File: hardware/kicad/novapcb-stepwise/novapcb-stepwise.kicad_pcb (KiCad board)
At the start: 6 copper layers, 105 x 85 mm, 129 parts, among them J1 USB-C_2.0, J10 CRSF_solder_pad, J11 ESC_solder_pad, J12 ESC_solder_pad, J13 ESC_solder_pad, J14 ESC_solder_pad, J15 ESC_solder_pad, J16 ESC_solder_pad, J17 ESC_solder_pad, J18 ESC_solder_pad, J19 MAUCH2_6P, J2 microSD_DM3AT, J20 CAN_4P, J3 TELEM_6P, J4 MAUCH_6P, J5 GPS_MAG_10P, J9 SWD_10P, Q2 AO3401A, Q3 AO4262E, Q4 AO4262E, Q5 AO3400A, U1 STM32H743VITx, U11 LM74700-Q1, U12 LM74700-Q1, U13 LP5907MFX-3.3, U14 TJA1051TK/3, U15 PESD2CAN, U2 AP2112K-3.3, U3 ICM-42688-P_LGA-14_2.5x3mm_P0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, U4 DPS310, U5 USBLC6-2P6, U6 TPS25940A, U7 LPS22HB, U8 BMI088, U9 LSM6DSV16X, Y1 8MHz

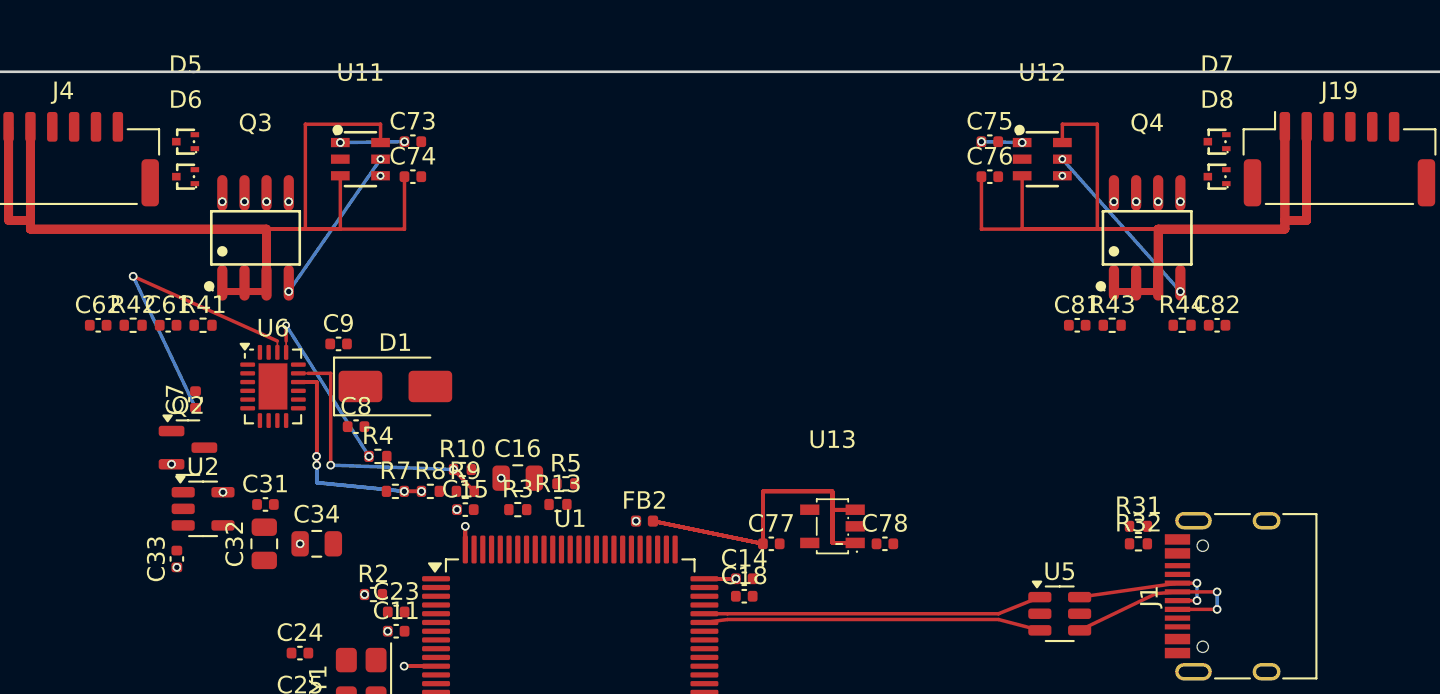
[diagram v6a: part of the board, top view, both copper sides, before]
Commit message: hw: Option B step 3 — U2 area re-layout + 4 sense-row mirror fixes
Per master 2026-05-23 sign-off on sch/option-b-buck sha ba91b16.
Single sweep: buck-discipline re-layout + sense-row symmetry close.

**Why**: Step 3 closes Option B. U2 footprint must change SOT-23-5 →
DFN-10-1EP_3x3 with L1 + new Cin/Cout topology + FB divider; 4
mirror-pair deviations (5-9mm) caught by audit-hardening must drop
to ≤0.5mm per pcb.ai R2 hard rule.

**Changes**:
- step5_place_B.py: B_REFDES + L1/R47/R48; ANCHORS rewritten for buck
  discipline (U2 stays at 24,25 sweet-spot; L1 east, magnetic axis ⊥
  buck-IMU; C31/C32 Cin west of VIN; C33 Cout east of L1; C34 NE of U2
  for ≤3mm body-edge DECOUPLING; R47/R48 south for ≤5mm FB trace);
  place_order updated.
- step6_place_A.py: R43=81, R44=85, C81=83, C82=87 mirror exactly
  about X=52.5 (was 76/80/74/82, 5-9mm deviations).
- novapcb-stepwise.kicad_pcb: U2 SOT-23-5→DFN-10-1EP; C31/C32/C33/C34
  footprint+value swap to match Option B netlist (was 0402 1µF /
  0805 4.7µF; now 0805 10µF / 0402 100nF / 0805 22µF / 0402 100nF);
  L1/R47/R48 added with pad-net assignments from novapcb.net;
  stale +3V3 via at (25.137, 24.050) removed (clashed with new U2
  pad 9 SW + pad 11 EP).
- fix_option_b_footprints.py: SWIG-safe 2-phase footprint patcher
  (pre-load → board-Add → subprocess → pad-net assign) — KiCad 9
  FootprintLoad regression after LoadBoard required this split.
- renders/option-b-step3/: top/bot/In2/In3 visual proof.

**Gates**:
- gate12_thermal @ all-actual positions: ALL PASS. Tj_U1=68.94°C
  (margin +11.1°C vs 80°C target; Option A was failing 82.5°C).
  Tj_U2=68.86°C. Energy balance +0.28%.
- audit_layout_compliance: 11/11 MIRROR_PAIRS PASS (sense-row deltas
  exactly 0.000mm); U2 DECOUPLING PASS (C34 @ 2.32mm body-edge);
  R1/R2/R3 buckets all green. FAIL count 4→3 (only pre-existing U5
  VBUS task #92 + U6 task #91 remain — both tracked sub-steps).
- gate14_drc: 0 new violations from Option B. 10 pre-existing
  drill_out_of_ra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
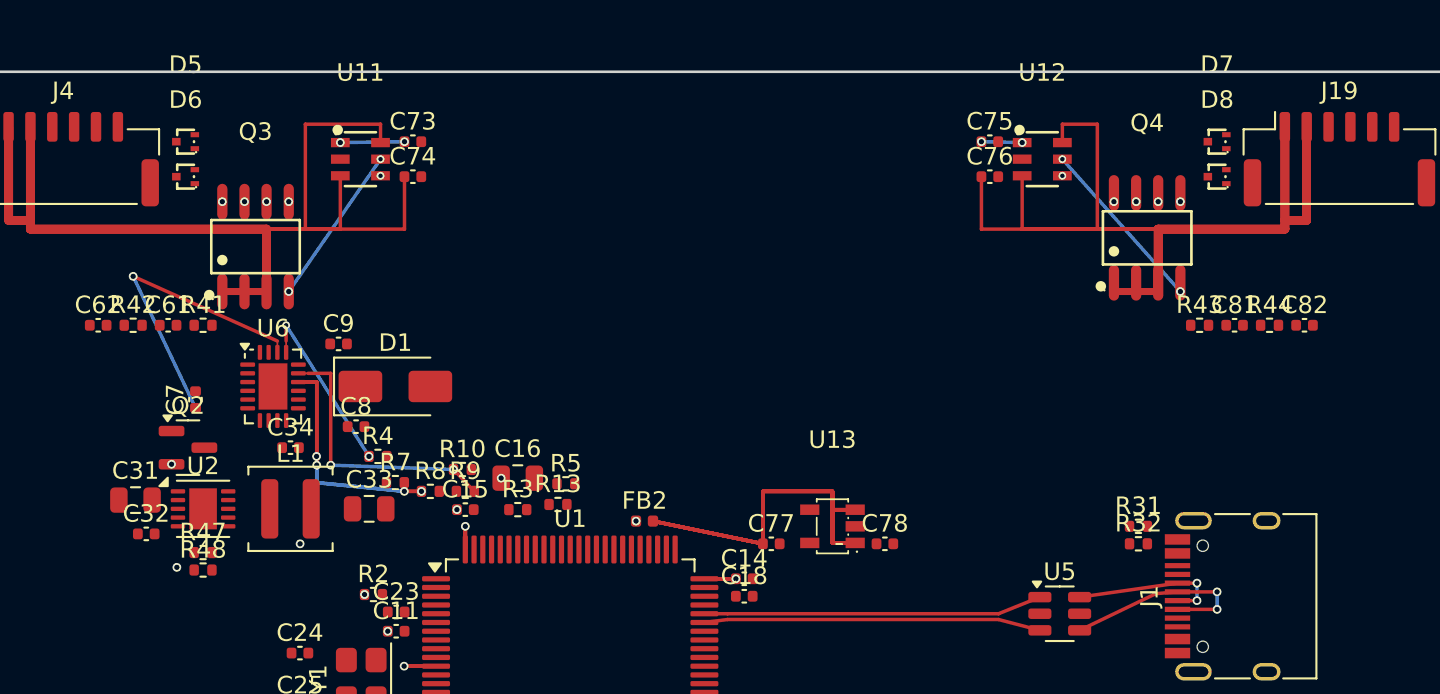
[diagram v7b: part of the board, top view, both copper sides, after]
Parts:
- added L1: 2.2uH XAL4020, L_Coilcraft_XAL4020-XXX, F.Cu at (29.0, 25.0)
- added R47: 562k, R_0402_1005Metric, F.Cu at (24.0, 27.5)
- added R48: 180k, R_0402_1005Metric, F.Cu at (24.0, 28.5)
- C31: value 1uF -> 10uF; footprint Capacitor_SMD:C_0402_1005Metric -> C_0805_2012Metric
- C32, C34: value 4.7uF -> 100nF; footprint Capacitor_SMD:C_0805_2012Metric -> C_0402_1005Metric
- C33: value 1uF -> 22uF; footprint Capacitor_SMD:C_0402_1005Metric -> C_0805_2012Metric
- U2: value AP2112K-3.3 -> TPS62177DQC; footprint Package_TO_SOT_SMD:SOT-23-5 -> DFN-10-1EP_3x3mm_P0.5mm_EP1.58x2.35mm
- moved C33 11.4 mm to (33.5, 25.0), turned to 0 degrees
- moved C81 9.00 mm to (83.0, 14.5)
- moved C31 7.44 mm to (20.1, 24.5)
- moved C32 6.77 mm to (20.8, 26.4), turned to 0 degrees
- moved C34 5.70 mm to (29.0, 21.5)
- moved C82 5.00 mm to (87.0, 14.5)
- moved R43 5.00 mm to (81.0, 14.5)
- moved R44 5.00 mm to (85.0, 14.5)
- moved Q3 0.50 mm to (27.0, 10.0)
- moved R7 0.50 mm to (35.0, 23.5)
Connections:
- U2 pad 1: +5V -> GND
- U2 pad 2: GND -> +5V
- U2 pad 5: +3V3 -> U2_FB
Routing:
- net +3V3: vias 21 -> 20

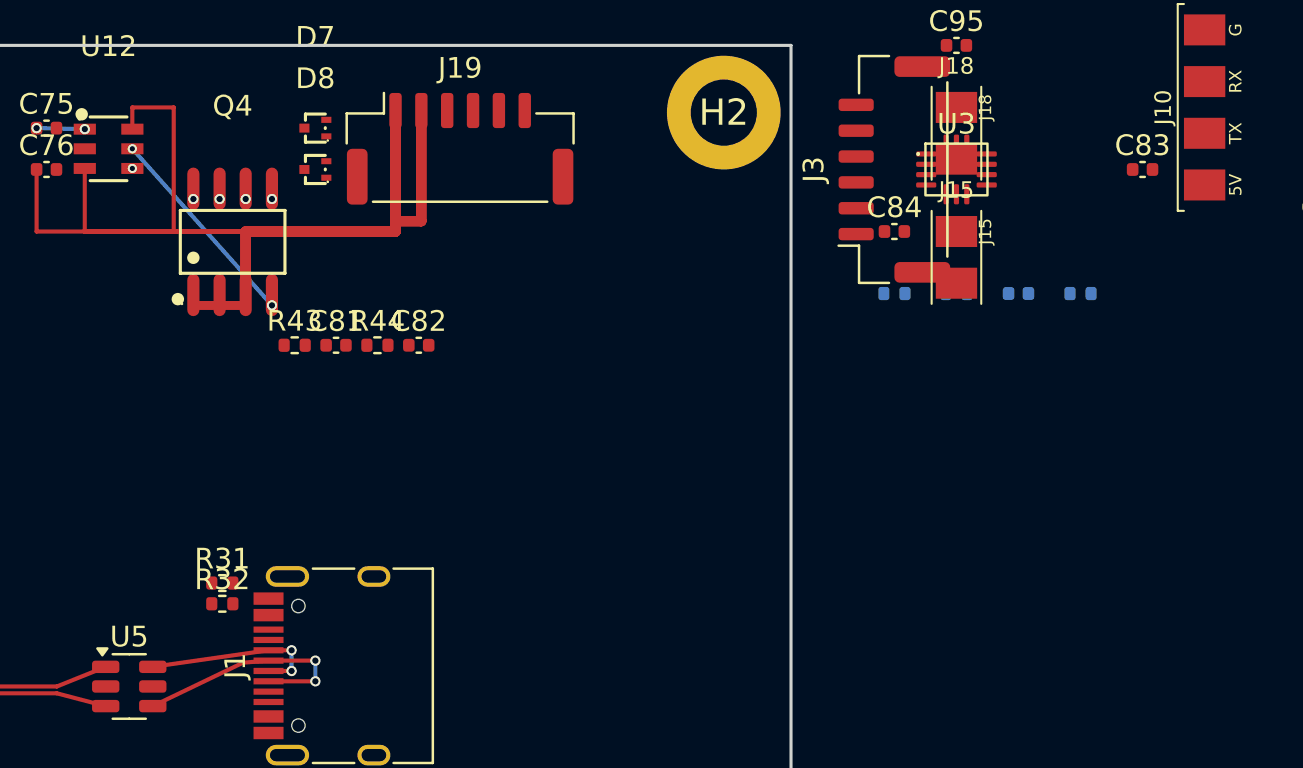
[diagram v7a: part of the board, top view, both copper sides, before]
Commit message: hw: U5 VBUS decap — add C83 100nF NW of U5 (master #27)
UNHALT step 1 per master 2026-05-23 carry-on directive. Closes the
pre-existing U5 DECOUPLING audit FAIL (was: nearest +5V cap C9 @ 43mm
body-edge — far too distant for an ESD chip's VBUS pin).

C83 (100nF 0402, +5V/GND, already in netlist) parked at X=122 — now
positioned at (74.5, 28.5) on the board:
- NORTH of U5 body (U5 N edge Y=29.27, C83 S edge Y=28.98 → 0.3mm gap)
- 2.4mm body-edge to U5 pad 5 (+5V VBUS) at global (74.138, 31.0) —
  within 3mm DECOUPLING rule
- Clear of R31/R32 (CC pulldowns at X=77.5, Y=26-27)
- Clear of USBC_D_M_PRE diff-pair routing at Y=31.95 east of U5

First attempt at (76.5, 31.0) caused 1 shorting + 2 solder-mask-bridge
violations against the USBC_D_M_PRE track east of U5 (track centerline
Y=31.95, length 4.84mm). NW placement redo bypasses the trace entirely.

Results:
- audit DECOUPLING: 4→3→2 (only pre-existing U6 task #91 remains)
- gate14 DRC: 10 → 13 (first attempt) → 10 (after redo) — back to
  pre-existing baseline (10 DRU coverage gaps from #87/#89, task #97)
- 0 net new DRC violations

Co-Authored-By: Claude Opus 4.7 <noreply@anthropic.com>
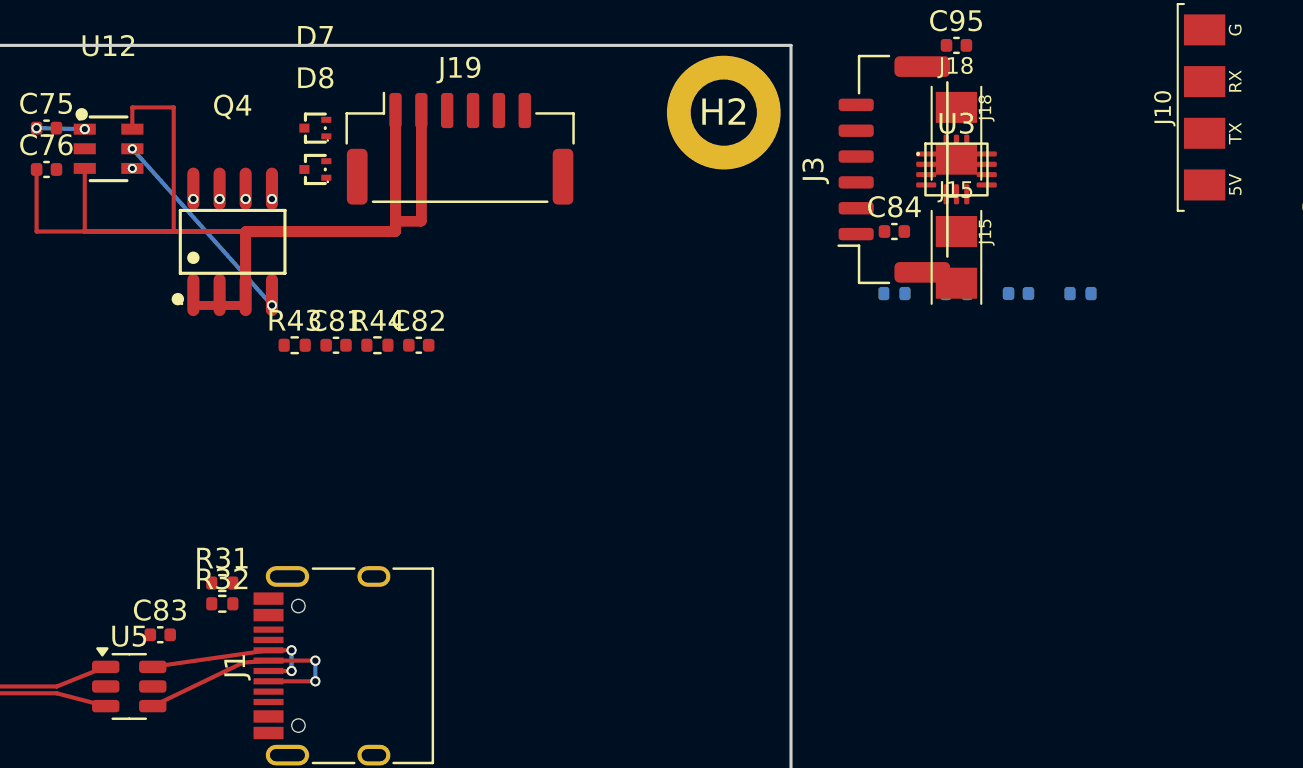
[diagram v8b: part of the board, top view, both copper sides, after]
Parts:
- moved C83 52.6 mm to (74.5, 28.5)
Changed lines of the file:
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@@
 	(footprint "Capacitor_SMD:C_0402_1005Metric"
 		(layer "F.Cu")
-		(at 122 6)
+		(at 74.5 28.5)
 		(descr "Capacitor SMD 0402 (1005 Metric), square (rectangular) end terminal, IPC-7351 nominal, (Body size source: IPC-SM-782 page 76, https://www.pcb-3d.com/wordpress/wp-content/uploads/ipc-sm-782a_amendment_1_and_2.pdf), generated with kicad-footprint-generator")
 		(tags "capacitor")
